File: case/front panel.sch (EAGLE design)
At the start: 5 parts

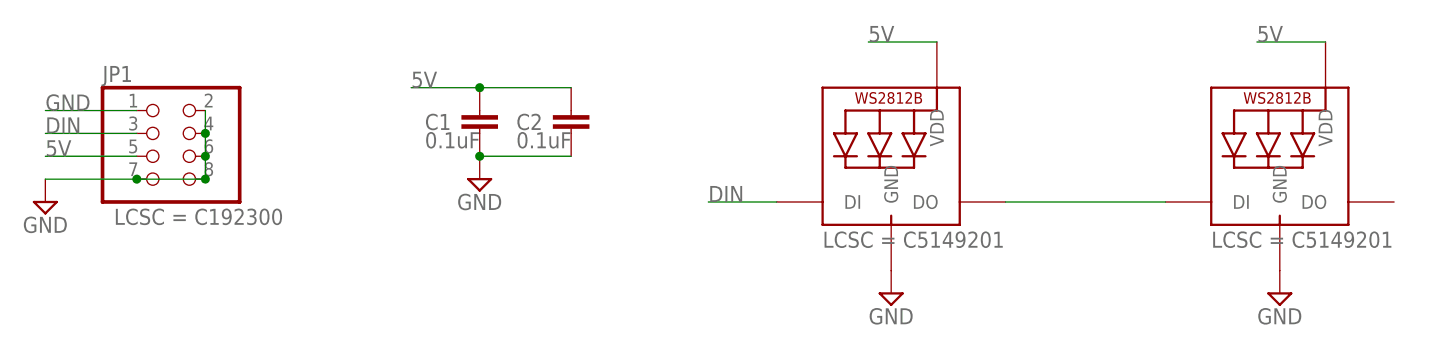
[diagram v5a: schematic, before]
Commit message: add light pipe holes and remove leds
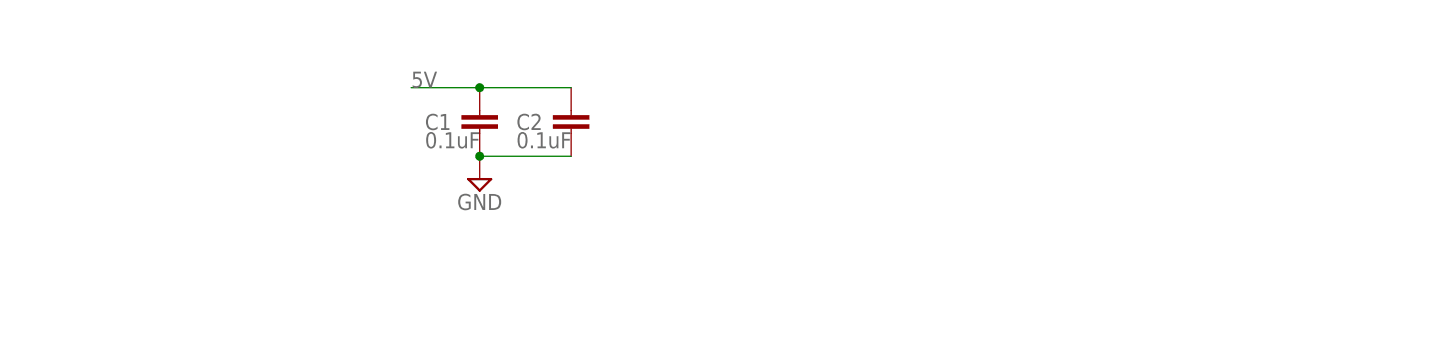
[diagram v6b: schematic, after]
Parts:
- removed JP1: connect, pinhead+:PINHD-2X4SMT
- removed LED0, LED1: WS2812B_SK6812E, microbuilder:WS2812B_SK6812E
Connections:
- removed net DIN: JP1.3, LED1.DI
- removed net N$2: LED0.DI, LED1.DO
- net 5V: no longer JP1.5, LED0.VDD, LED1.VDD
- net GND: no longer JP1.1, JP1.2, JP1.4, JP1.6, JP1.7, JP1.8, LED0.GND, LED1.GND
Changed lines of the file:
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@@
 <part name="C1" library="Nordic_nRF" library_urn="urn:adsk.eagle:library:169009" deviceset="CAPACITOR" device="_0805_N" package3d_urn="urn:adsk.eagle:package:2593736/1" value="0.1uF"/>
 <part name="SUPPLY1" library="Power_Symbols" library_urn="urn:adsk.eagle:library:16502351" deviceset="GND" device="" value="GND"/>
-<part name="SUPPLY2" library="Power_Symbols" library_urn="urn:adsk.eagle:library:16502351" deviceset="GND" device="" value="GND"/>
-<part name="SUPPLY3" library="Power_Symbols" library_urn="urn:adsk.eagle:library:16502351" deviceset="GND" device="" value="GND"/>
-<part name="SUPPLY4" library="Power_Symbols" library_urn="urn:adsk.eagle:library:16502351" deviceset="GND" device="" value="GND"/>
 <part name="C2" library="Nordic_nRF" library_urn="urn:adsk.eagle:library:169009" deviceset="CAPACITOR" device="_0805_N" package3d_urn="urn:adsk.eagle:package:2593736/1" value="0.1uF"/>
-<part name="LED1" library="microbuilder" deviceset="WS2812B" device="_SK6812E">
-<attribute name="LCSC" value="C5149201"/>
-</part>
-<part name="LED0" library="microbuilder" deviceset="WS2812B" device="_SK6812E">
-<attribute name="LCSC" value="C5149201"/>
-</part>
-<part name="JP1" library="pinhead+" deviceset="PINHD-2X4" device="SMT" value="connect">
-<attribute name="LCSC" value="C192300"/>
-</part>
 </parts>
 <sheets>
@@
 <attribute name="VALUE" x="22.86" y="17.78" size="1.778" layer="96" align="center"/>
 </instance>
-<instance part="SUPPLY2" gate="G$1" x="68.58" y="7.62" smashed="yes">
-<attribute name="VALUE" x="68.58" y="5.08" size="1.778" layer="96" align="center"/>
-</instance>
-<instance part="SUPPLY3" gate="G$1" x="111.76" y="7.62" smashed="yes">
-<attribute name="VALUE" x="111.76" y="5.08" size="1.778" layer="96" align="center"/>
-</instance>
-<instance part="SUPPLY4" gate="G$1" x="-25.4" y="17.78" smashed="yes">
-<attribute name="VALUE" x="-25.4" y="15.24" size="1.778" layer="96" align="center"/>
-</instance>
 <instance part="C2" gate="C$1" x="33.02" y="27.94" smashed="yes">
 <attribute name="NAME" x="26.924" y="25.781" size="1.778" layer="95"/>
 <attribute name="VALUE" x="26.924" y="23.749" size="1.778" layer="96"/>
-</instance>
-<instance part="LED1" gate="G$1" x="68.58" y="20.32" smashed="yes">
-<attribute name="LCSC" x="60.96" y="12.7" size="1.778" layer="96" display="both"/>
-</instance>
-<instance part="LED0" gate="G$1" x="111.76" y="20.32" smashed="yes">
-<attribute name="LCSC" x="104.14" y="12.7" size="1.778" layer="96" display="both"/>
-</instance>
-<instance part="JP1" gate="A" x="-12.7" y="22.86" smashed="yes">
-<attribute name="NAME" x="-19.05" y="31.115" size="1.778" layer="95"/>
-<attribute name="LCSC" x="-17.78" y="15.24" size="1.778" layer="96" display="both"/>
 </instance>
 </instances>
@@
 <junction x="22.86" y="22.86"/>
 </segment>
-<segment>
-<wire x1="-15.24" y1="20.32" x2="-25.4" y2="20.32" width="0.1524" layer="91"/>
-<pinref part="SUPPLY4" gate="G$1" pin="GND"/>
-<pinref part="JP1" gate="A" pin="7"/>
-<pinref part="JP1" gate="A" pin="2"/>
-<pinref part="JP1" gate="A" pin="4"/>
-<wire x1="-7.62" y1="27.94" x2="-7.62" y2="25.4" width="0.1524" layer="91"/>
-<pinref part="JP1" gate="A" pin="6"/>
-<wire x1="-7.62" y1="25.4" x2="-7.62" y2="22.86" width="0.1524" layer="91"/>
-<junction x="-7.62" y="25.4"/>
-<pinref part="JP1" gate="A" pin="8"/>
-<wire x1="-7.62" y1="22.86" x2="-7.62" y2="20.32" width="0.1524" layer="91"/>
-<junction x="-7.62" y="22.86"/>
-<wire x1="-7.62" y1="20.32" x2="-15.24" y2="20.32" width="0.1524" layer="91"/>
-<junction x="-7.62" y="20.32"/>
-<junction x="-15.24" y="20.32"/>
-</segment>
-<segment>
-<pinref part="LED1" gate="G$1" pin="GND"/>
-<pinref part="SUPPLY2" gate="G$1" pin="GND"/>
-</segment>
-<segment>
-<pinref part="SUPPLY3" gate="G$1" pin="GND"/>
-<pinref part="LED0" gate="G$1" pin="GND"/>
-</segment>
-<segment>
-<wire x1="-15.24" y1="27.94" x2="-25.4" y2="27.94" width="0.1524" layer="91"/>
-<label x="-25.4" y="27.94" size="1.778" layer="95"/>
-<pinref part="JP1" gate="A" pin="1"/>
-</segment>
 </net>
 <net name="5V" class="0">
@@
 <junction x="22.86" y="30.48"/>
 </segment>
-<segment>
-<wire x1="116.84" y1="35.56" x2="109.22" y2="35.56" width="0.1524" layer="91"/>
-<label x="109.22" y="35.56" size="1.778" layer="95"/>
-<pinref part="LED0" gate="G$1" pin="VDD"/>
-</segment>
-<segment>
-<wire x1="73.66" y1="35.56" x2="66.04" y2="35.56" width="0.1524" layer="91"/>
-<label x="66.04" y="35.56" size="1.778" layer="95"/>
-<pinref part="LED1" gate="G$1" pin="VDD"/>
-</segment>
-<segment>
-<pinref part="JP1" gate="A" pin="5"/>
-<wire x1="-15.24" y1="22.86" x2="-25.4" y2="22.86" width="0.1524" layer="91"/>
-<label x="-25.4" y="22.86" size="1.778" layer="95"/>
-</segment>
-</net>
-<net name="N$2" class="0">
-<segment>
-<wire x1="81.28" y1="17.78" x2="99.06" y2="17.78" width="0.1524" layer="91"/>
-<pinref part="LED1" gate="G$1" pin="DO"/>
-<pinref part="LED0" gate="G$1" pin="DI"/>
-</segment>
-</net>
-<net name="DIN" class="0">
-<segment>
-<wire x1="-15.24" y1="25.4" x2="-25.4" y2="25.4" width="0.1524" layer="91"/>
-<label x="-25.4" y="25.4" size="1.778" layer="95"/>
-<pinref part="JP1" gate="A" pin="3"/>
-</segment>
-<segment>
-<wire x1="55.88" y1="17.78" x2="48.26" y2="17.78" width="0.1524" layer="91"/>
-<label x="48.26" y="17.78" size="1.778" layer="95"/>
-<pinref part="LED1" gate="G$1" pin="DI"/>
-</segment>
 </net>
 </nets>
 </sheet>
 </sheets>
-<errors>
-</errors>
 </schematic>
 </drawing>
